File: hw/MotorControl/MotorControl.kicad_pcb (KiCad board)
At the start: 4 copper layers, 101 x 48 mm, 158 parts, among them J1 1733583, J2 B4B-EH-A(LF)(SN), J3 B6B-EH-A(LF)(SN), J4 430450412, Q1 IRF540N, Q2 IRF540N, Q3 IRF540N, Q4 IRF540N, Q5 IRF540N, Q6 IRF540N, SW1 BTSA-N-P-1, U1 STGAP2SCM, U10 AMC1200BDWV, U11 STM32L431CCTx, U12 TPS54202DDC, U13 AMC1200BDWV, U14 SN74LVC1G125DBV, U15 SN74LVC1G125DBV, U16 AMC1200BDWV, U2 STGAP2SCM, U3 STGAP2SCM, U4 AMC1200BDWV, U5 SN65HVD230, U6 TPS54202DDC, U7 STGAP2SCM, U8 STGAP2SCM, U9 STGAP2SCM, Y1 Crystal_GND24

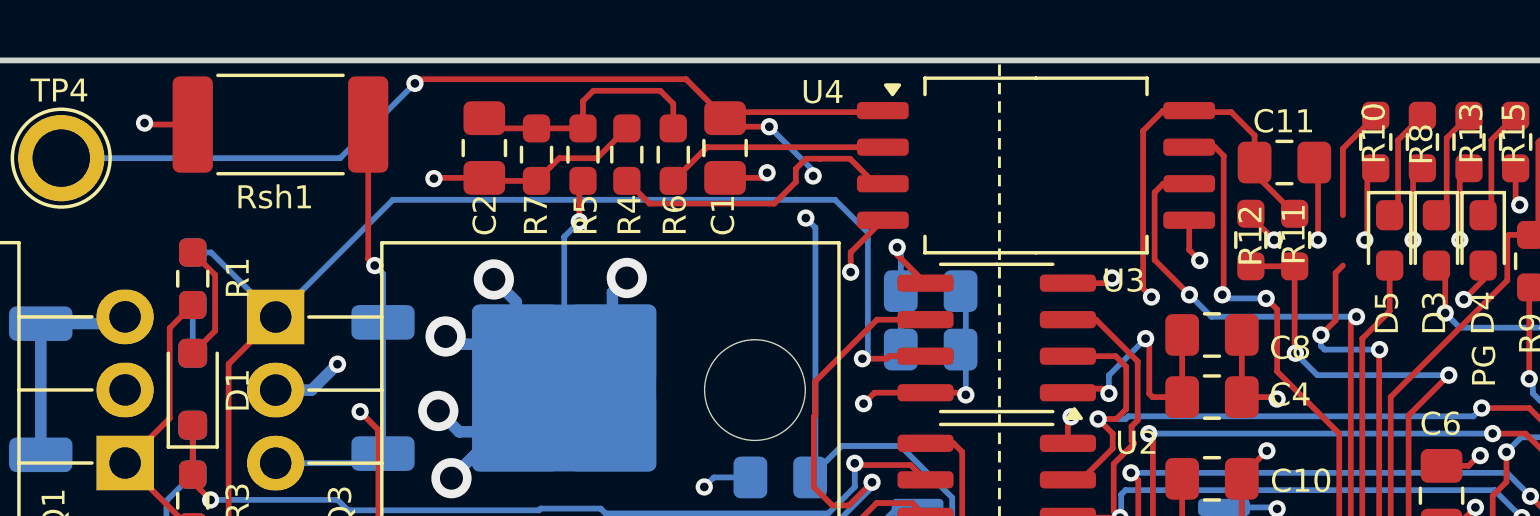
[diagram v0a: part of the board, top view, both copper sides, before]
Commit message: add pdf outputs
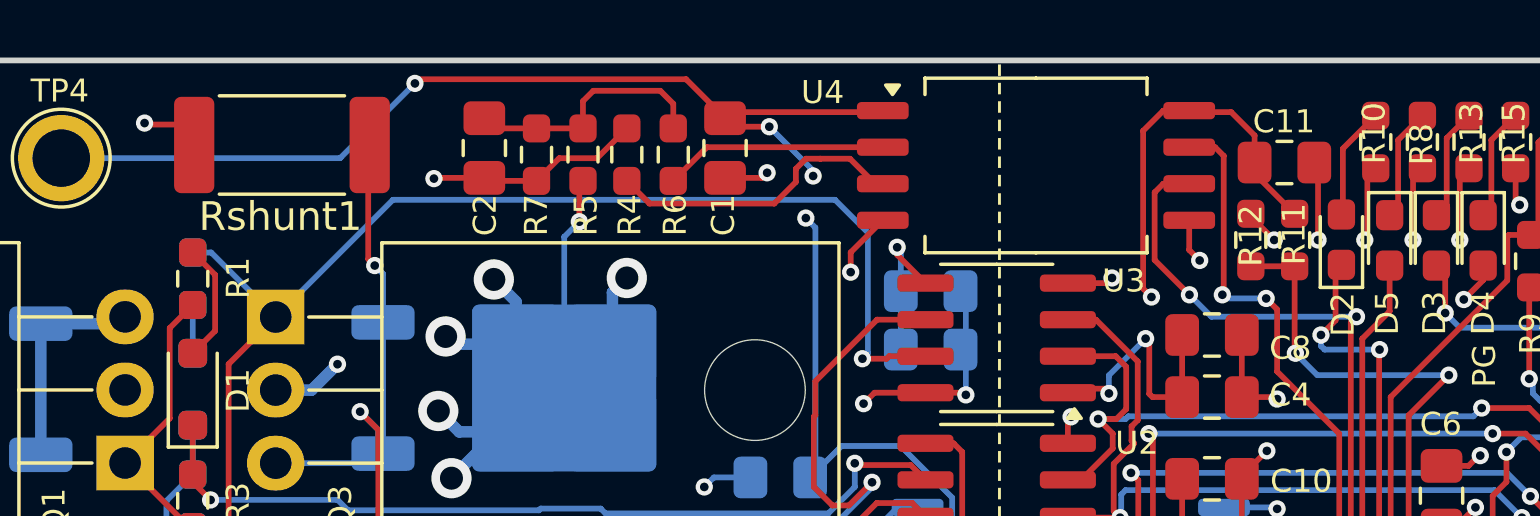
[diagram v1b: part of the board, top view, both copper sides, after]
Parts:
- removed Rsh1: HoLLR2512-3W-15mR-1%, Resistor_SMD:R_2512_6332Metric_Pad1.40x3.35mm_HandSolder
- added D2: KT-0603W, LED_SMD:LED_0603_1608Metric_Pad1.05x0.95mm_HandSolder, F.Cu at (145.0, 73.6)
- added Rshunt1: HoLLR2512-3W-15mR-1%, Resistor_SMD:R_2512_6332Metric_Pad1.40x3.35mm_HandSolder, F.Cu at (108.2, 70.4)
